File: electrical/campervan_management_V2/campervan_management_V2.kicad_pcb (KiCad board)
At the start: 4 copper layers, 130 x 150 mm, 177 parts, among them J1 Battery & Fuse, J10 Output Flow Sensor, J11 Input Flow Sensor, J2 Battery 2, J3 Solar Charge, J4 Power On/Off Switch, J5 RS485, J6 Fans, J7 Relays, J8 Temp, J9 Starter Battery, K1 G5V-2, Q1 FDS4685, Q2 FDS4685, Q3 FDS4685, Q4 FDS4685, Q5 FDS4685, Q6 FDS4685, Q7 MMBT2222A, Q8 MMBT2222A, SW1 SW_Push, U1 MCP16311x-xMNY, U10 LTV-817S-TA1-C, U11 LTV-817S-TA1-C, U12 LTV-817S-TA1-C, U13 LTV-817S-TA1-C, U14 LTV-817S-TA1-C, U15 LTV-817S-TA1-C, U16 LTV-817S-TA1-C, U17 LM358DR2G, U18 LM358DR2G, U19 HCNR200-500E, U2 MCP16311x-xMNY, U20 HCNR200-500E, U21 HCNR200-500E, U22 AMS1117-3.3/TLV761, U23 LM358DR2G, U24 LM358DR2G, U25 LM358DR2G, U3 LTV-817S-TA1-C, U4 LTV-817S-TA1-C, U5 AMS1117-3.3/TLV761, U6 LTV-817S-TA1-C, U7 LTV-817S-TA1-C, U8 MAX487E, U9 LTV-817S-TA1-C

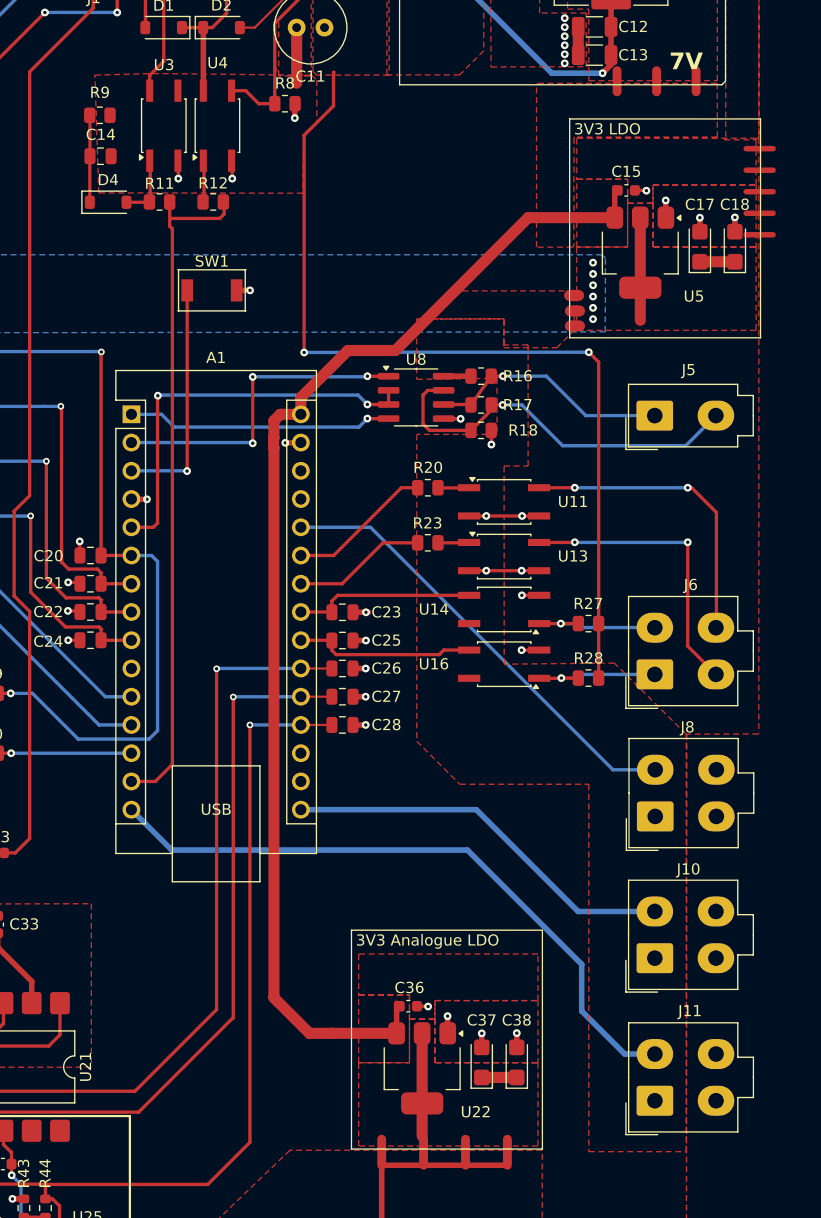
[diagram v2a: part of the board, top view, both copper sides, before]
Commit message: Added optocouplers to flow sensors
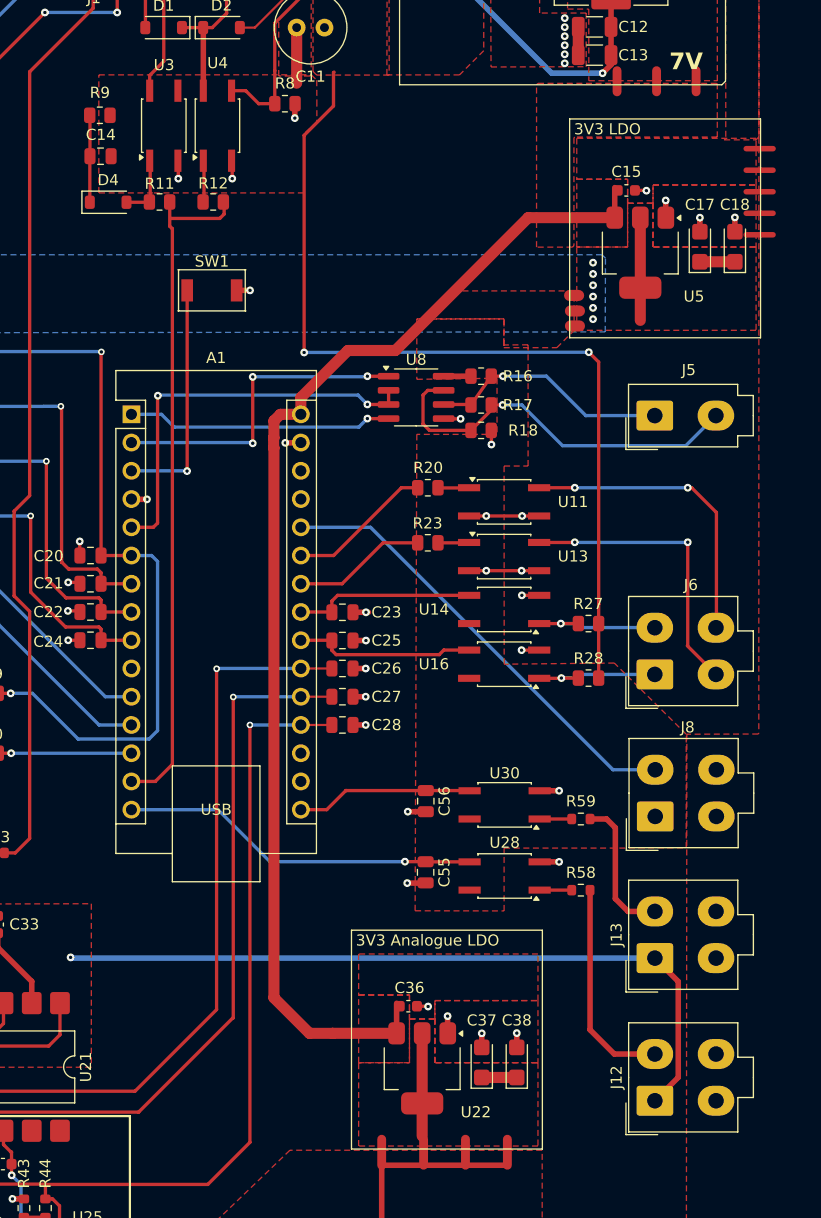
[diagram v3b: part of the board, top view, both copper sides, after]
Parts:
- removed J10: Output Flow Sensor, Connector_Molex:Molex_Mini-Fit_Jr_5566-04A_2x02_P4.20mm_Vertical
- removed J11: Input Flow Sensor, Connector_Molex:Molex_Mini-Fit_Jr_5566-04A_2x02_P4.20mm_Vertical
- added C55: 100nF, Capacitor_SMD:C_0805_2012Metric, F.Cu at (120.1, 124.4)
- added C56: 100nF, Capacitor_SMD:C_0805_2012Metric, F.Cu at (120.1, 118.0)
- added J12: Input Flow Sensor, Connector_Molex:Molex_Mini-Fit_Jr_5566-04A_2x02_P4.20mm_Vertical, F.Cu at (140.7, 145.0)
- added J13: Output Flow Sensor, Connector_Molex:Molex_Mini-Fit_Jr_5566-04A_2x02_P4.20mm_Vertical, F.Cu at (140.7, 132.1)
- added R58: 5k6, Resistor_SMD:R_0603_1608Metric, F.Cu at (134.0, 126.0)
- added R59: 5k6, Resistor_SMD:R_0603_1608Metric, F.Cu at (134.0, 119.6)
- added U28: LTV-817S-TA1-C, Package_SO:SO-4_4.4x3.6mm_P2.54mm, F.Cu at (127.2, 124.8)
- added U30: LTV-817S-TA1-C, Package_SO:SO-4_4.4x3.6mm_P2.54mm, F.Cu at (127.2, 118.4)
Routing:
- net VIN: track 166.9 -> 234.1 mm, vias 4 -> 5
- net /Input Flow Sensor: track 58.6 -> 32.4 mm, vias 0 -> 1
- net /Output Flow Sensor: track 35.6 -> 15.9 mm
- net Net-(J12-Pin_2): track 0.00 -> 19.3 mm
- net Net-(J13-Pin_2): track 0.00 -> 13.0 mm
- net GND: track 148.3 -> 155.1 mm, vias 96 -> 100
- net Net-(R58-Pad2): track 0.00 -> 2.89 mm
- net Net-(R59-Pad2): track 0.00 -> 2.88 mm

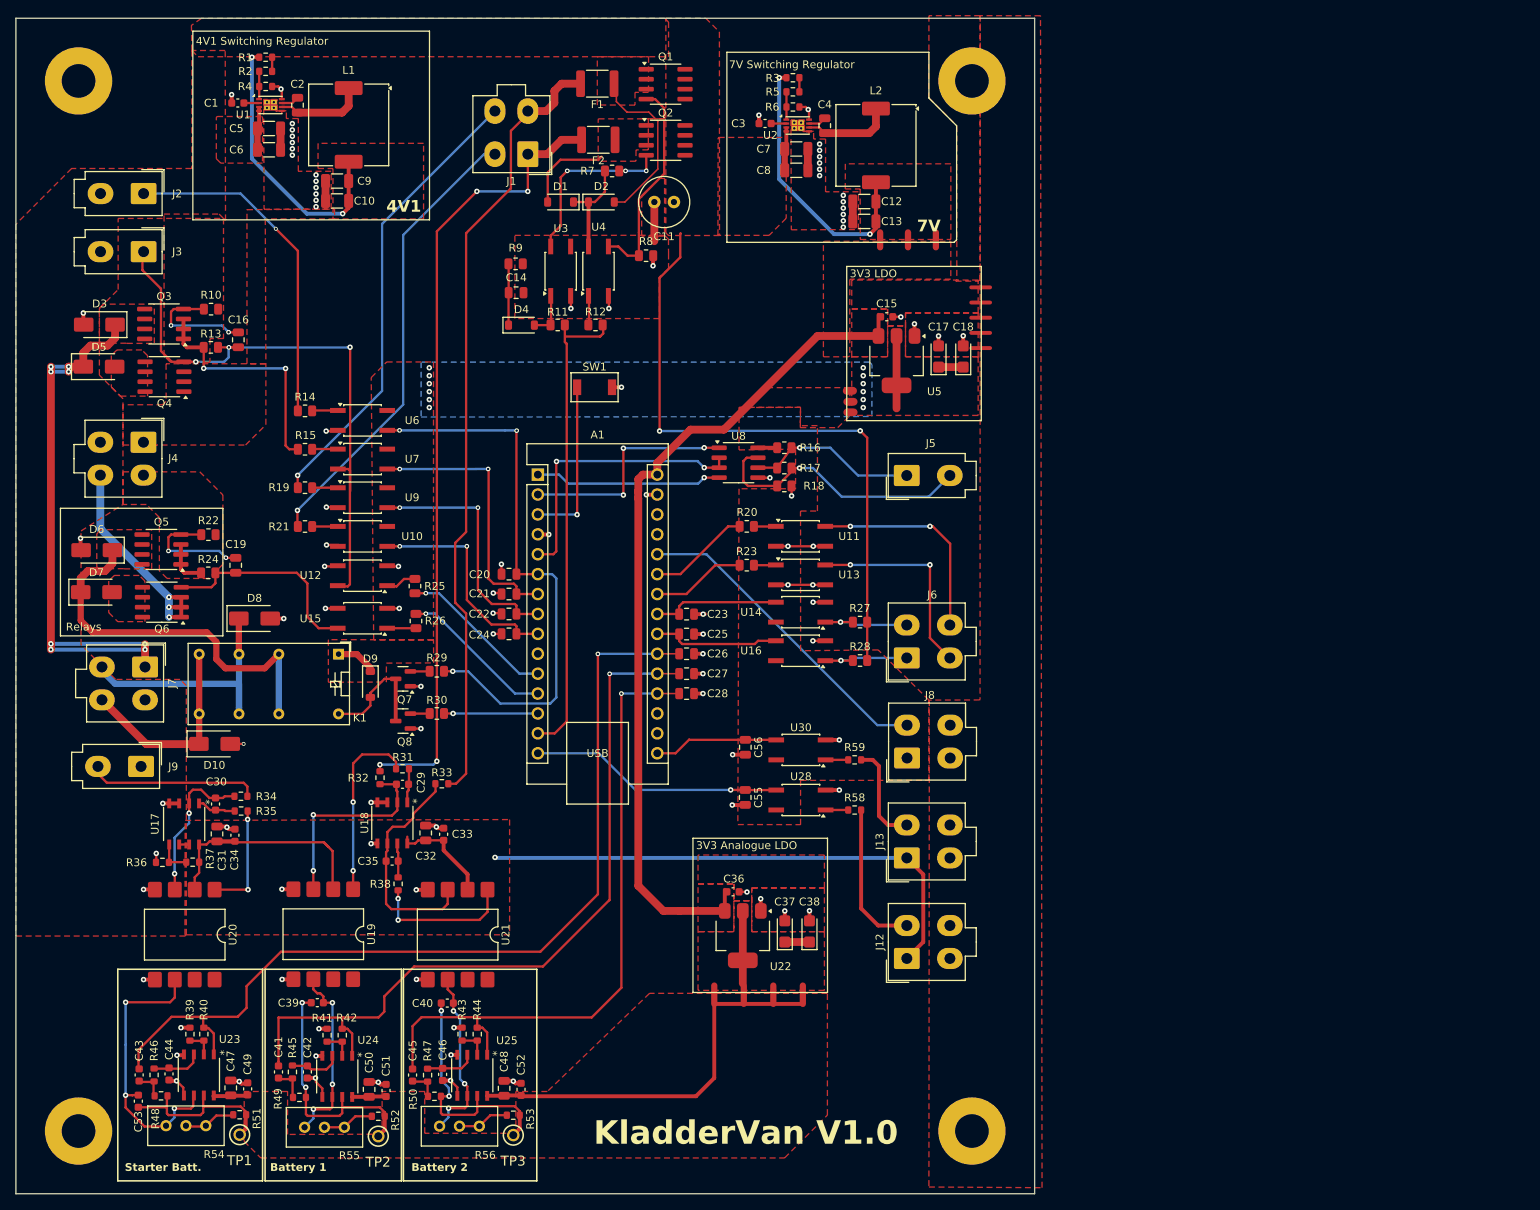
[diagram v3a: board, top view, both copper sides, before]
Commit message: updated 4V1 switcher resistor values. Clean up and reannotate PCB
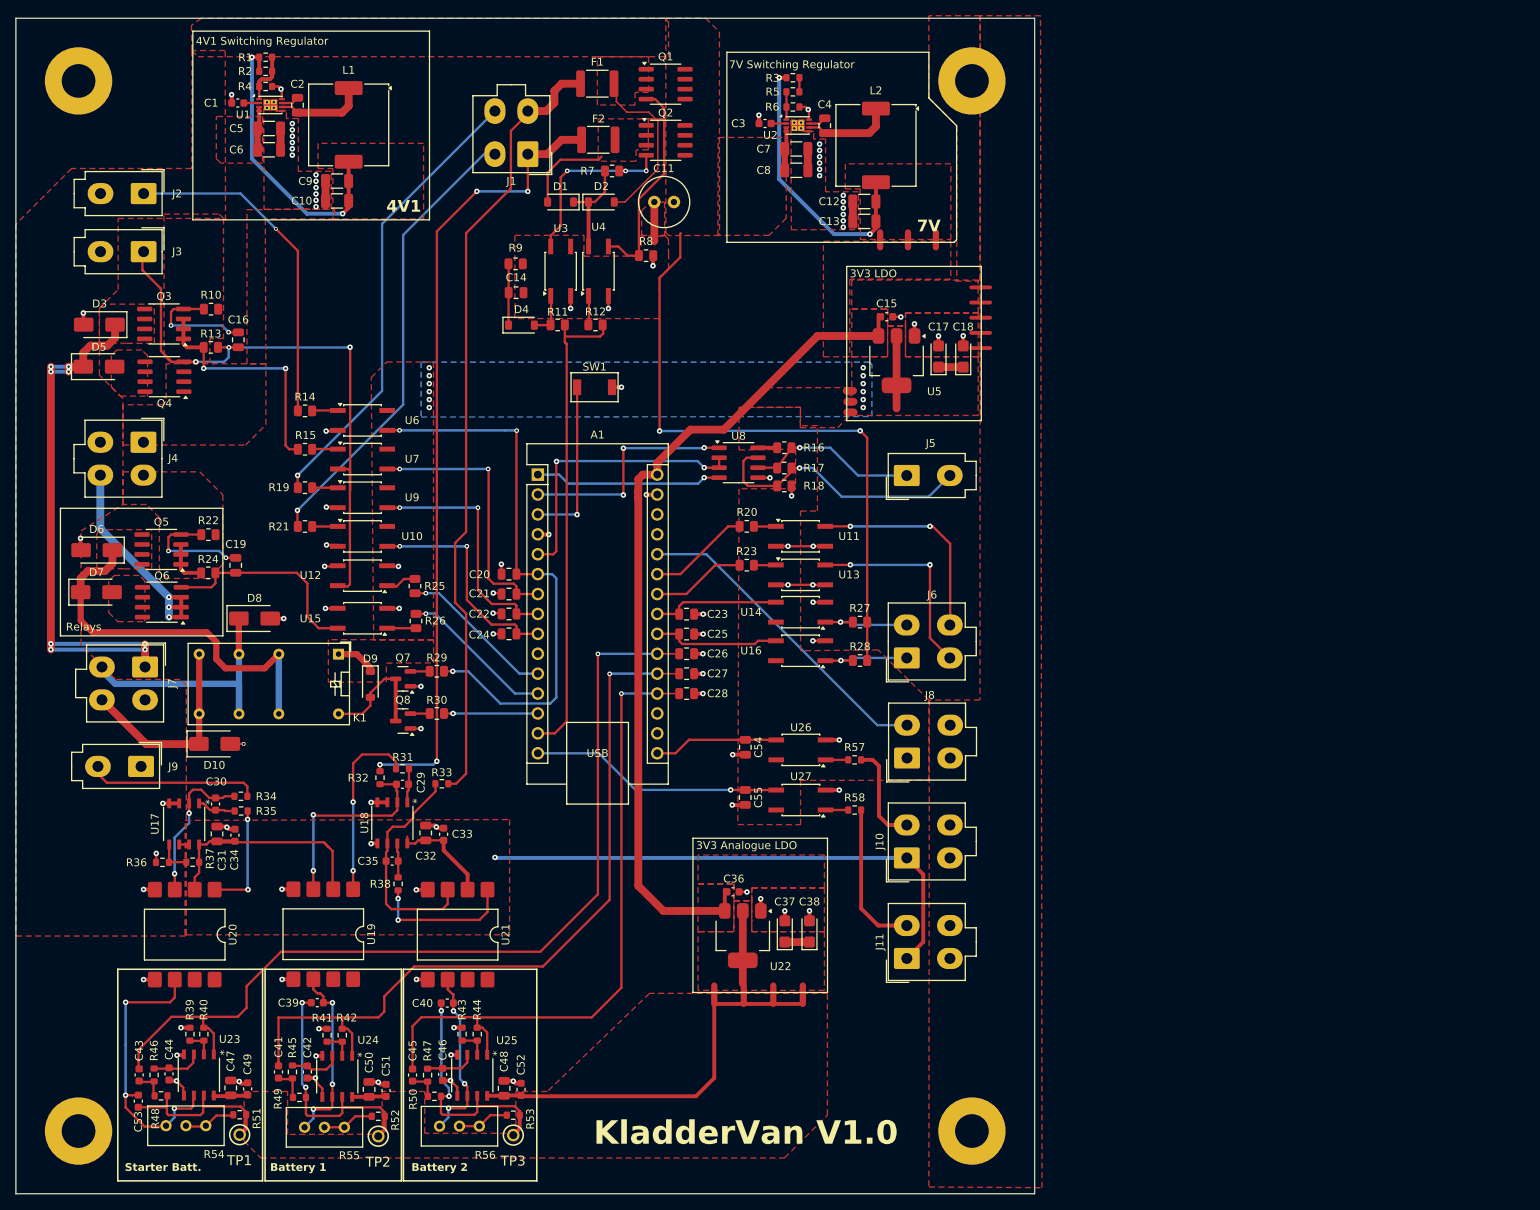
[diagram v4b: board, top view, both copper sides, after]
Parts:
- R1: value 68k -> 330k
- R2: value 10k -> 47k
- turned R2 to 0 degrees
- renumbered C56 to C54, J13 to J10, J12 to J11, R59 to R57, U30 to U26, U28 to U27
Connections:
- R1 pad 2: Net-(R1-Pad2) -> Net-(U1-Vfb)
- R2 pad 1: Net-(R1-Pad2) -> VCC_4V1
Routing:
- net Net-(U1-Vfb): track 3.45 -> 6.56 mm
- net Net-(R1-Pad2): track 1.80 -> 0.00 mm
- net VCC_4V1: track 35.3 -> 37.1 mm
